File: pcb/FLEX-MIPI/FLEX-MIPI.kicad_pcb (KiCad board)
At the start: 2 copper layers, 2 parts, among them CN1 OK-23GF030-04, J1 Conn_01x22

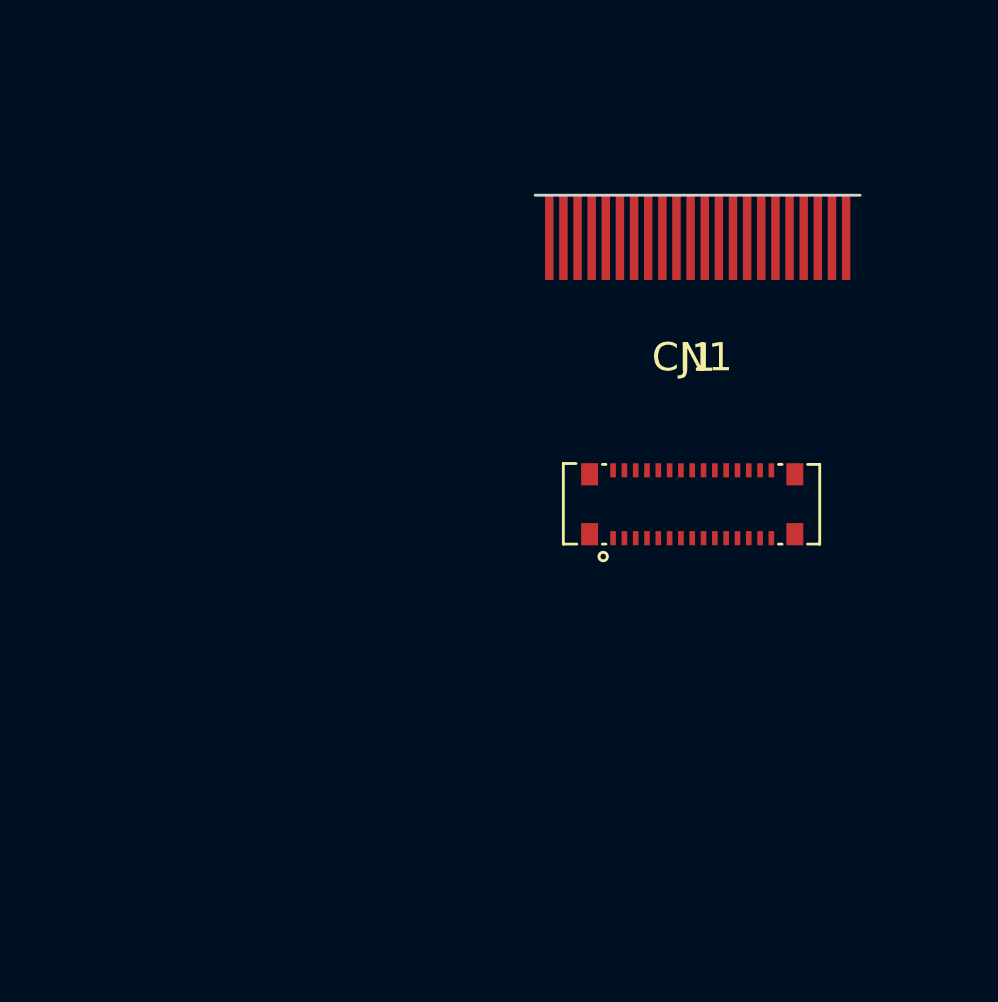
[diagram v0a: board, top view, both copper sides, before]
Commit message: flex mipi work
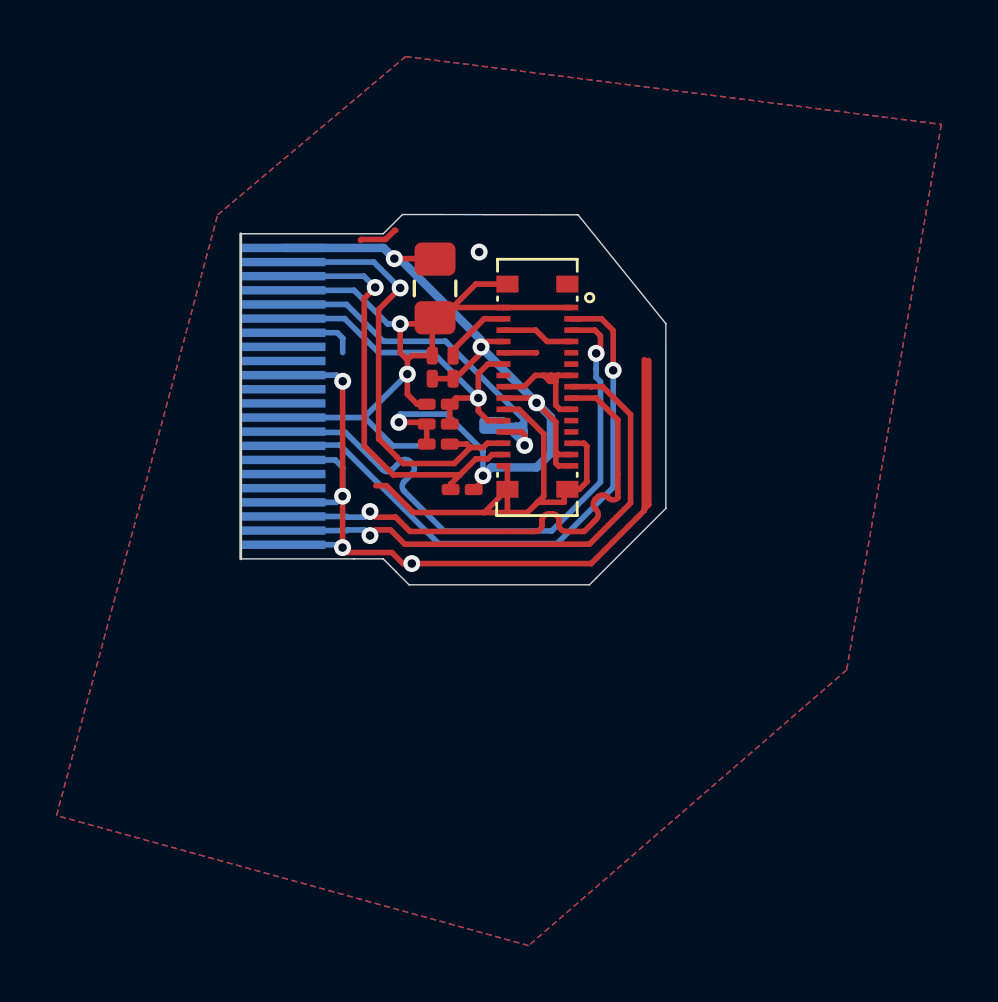
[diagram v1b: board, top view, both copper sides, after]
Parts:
- added C1: 10uF, Capacitor_SMD:C_0805_2012Metric_Pad1.18x1.45mm_HandSolder, F.Cu at (93.7, 53.1)
- added C2: 0.1uF, Capacitor_SMD:C_0201_0603Metric_Pad0.64x0.40mm_HandSolder, F.Cu at (93.6, 55.9)
- added C3: 0.1uF, Capacitor_SMD:C_0201_0603Metric_Pad0.64x0.40mm_HandSolder, F.Cu at (93.8, 57.2)
- added R1: R, Resistor_SMD:R_0201_0603Metric_Pad0.64x0.40mm_HandSolder, F.Cu at (94.6, 60.2)
- added R2: R, Resistor_SMD:R_0201_0603Metric_Pad0.64x0.40mm_HandSolder, F.Cu at (93.8, 58.6)
- added R3: R, Resistor_SMD:R_0201_0603Metric_Pad0.64x0.40mm_HandSolder, F.Cu at (94.3, 55.9)
- added R4: R, Resistor_SMD:R_0201_0603Metric_Pad0.64x0.40mm_HandSolder, F.Cu at (93.8, 57.9)
- added TP1: TestPoint, TestPoint_SMD_1.0x0.6mm_Flex:TestPoint_SMD_1.0x0.6mm_Flex, B.Cu at (95.8, 58.0)
- J1: moved to B.Cu
- moved J1 17.7 mm to (86.8, 56.9), turned to -90 degrees
- moved CN1 6.88 mm to (97.3, 56.6), turned to 90 degrees
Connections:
- net /CTP_RST renamed /RST
- CN1 pad : (no net) -> GND
- CN1 pad 14: unconnected-(CN1-Pad14) -> /LCM_ID
- CN1 pad 24: /CTP_INT -> /TP_INT
- J1 pad 5: /VCI_EN -> /TP_INT
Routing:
- net GND: track 0.00 -> 95.9 mm, vias 0 -> 7
- net +3V3: track 0.00 -> 32.7 mm, vias 0 -> 5
- net /LCM_CLKN: track 0.00 -> 21.2 mm, vias 0 -> 1
- net /LCM_CLKP: track 0.00 -> 21.1 mm, vias 0 -> 1
- net /LCM_D0N: track 0.00 -> 18.9 mm, vias 0 -> 1
- net /LCM_D0P: track 0.00 -> 18.8 mm, vias 0 -> 1
- net /TP_INT: track 0.00 -> 17.6 mm, vias 0 -> 1
- net /TP_TWI2_SDA: track 0.00 -> 16.0 mm, vias 0 -> 1
- net /TP_TWI2_SCK: track 0.00 -> 15.5 mm, vias 0 -> 1
- net /RST: track 0.00 -> 13.3 mm, vias 0 -> 1
- net /VCI_EN: track 0.00 -> 2.44 mm
- added copper zone on B.Cu, net GND
- added copper zone on F.Cu, net GND
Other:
- board outline added: 15 x 13.1 mm

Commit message: pcb fixes
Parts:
- removed TP1: TestPoint, TestPoint_SMD_1.0x0.6mm_Flex:TestPoint_SMD_1.0x0.6mm_Flex
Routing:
- net /TP_INT: track 17.6 -> 13.4 mm
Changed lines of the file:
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@@
 		)
-	)
-	(footprint "TestPoint_SMD_1.0x0.6mm_Flex:TestPoint_SMD_1.0x0.6mm_Flex"
-		(layer "B.Cu")
-		(at 95.75 57.95)
-		(descr "Compact hand-solder test pad for flex PCB; 1.0 x 0.6 mm rounded copper, 0.10 mm coverlay/mask expansion, no paste aperture")
-		(tags "test point flex FPC hand solder wire compact")
-		(property "Reference" "TP1"
-			(at 0 1.1 180)
-			(layer "B.Fab")
-			(hide yes)
-			(effects
-				(font
-					(size 0.6 0.6)
-					(thickness 0.1)
-				)
-				(justify mirror)
-			)
-		)
-		(property "Value" "TestPoint"
-			(at 0 -1.1 180)
-			(layer "B.Fab")
-			(hide yes)
-			(effects
-				(font
-					(size 0.6 0.6)
-					(thickness 0.1)
-				)
-				(justify mirror)
-			)
-		)
-		(property "Datasheet" ""
-			(at 0 0 180)
-			(layer "B.Fab")
-			(hide yes)
-			(effects
-				(font
-					(size 1.27 1.27)
-				)
-				(justify mirror)
-			)
-		)
-		(property "Description" "test point"
-			(at 0 0 180)
-			(layer "B.Fab")
-			(hide yes)
-			(effects
-				(font
-					(size 1.27 1.27)
-				)
-				(justify mirror)
-			)
-		)
-		(property ki_fp_filters "Pin* Test*")
-		(sheetname "/")
-		(sheetfile "FLEX-MIPI.kicad_sch")
-		(units
-			(unit
-				(name "A")
-				(pins "1")
-			)
-		)
-		(attr smd)
-		(duplicate_pad_numbers_are_jumpers no)
-		(pad "1" smd roundrect
-			(at 0 0)
-			(size 1 0.6)
-			(layers "B.Cu" "B.Mask")
-			(roundrect_rratio 0.25)
-			(net "/TP_INT")
-			(pinfunction "1_1")
-			(pintype "passive")
-			(solder_mask_margin 0.1)
-		)
-		(embedded_fonts no)
 	)
 	(footprint "Flex_Tails:FPC_Tail_22P_P0.5"
@@
 	(segment
 		(start 96.860002 58.657258)
-		(end 97.028 58.48926)
-		(width 0.2)
-		(layer "B.Cu")
-		(net "/TP_INT")
-	)
-	(segment
-		(start 96.860002 58.657258)
 		(end 96.860002 58.260002)
-		(width 0.2)
-		(layer "B.Cu")
-		(net "/TP_INT")
-	)
-	(segment
-		(start 95.75 57.95)
-		(end 96.3 57.95)
-		(width 0.2)
-		(layer "B.Cu")
-		(net "/TP_INT")
-	)
-	(segment
-		(start 96.681475 57.95)
-		(end 96.860002 57.771473)
 		(width 0.2)
 		(layer "B.Cu")
@@
 	)
 	(segment
-		(start 96.857258 58.657258)
-		(end 96.3 58.1)
-		(width 0.2)
-		(layer "B.Cu")
-		(net "/TP_INT")
-	)
-	(segment
 		(start 96.860002 58.657258)
 		(end 96.860002 58.128527)
@@
 	)
 	(segment
-		(start 95.75 57.95)
-		(end 96.55 57.95)
-		(width 0.2)
-		(layer "B.Cu")
-		(net "/TP_INT")
-	)
-	(segment
 		(start 94.060529 54.972)
 		(end 96.860002 57.771473)
@@
 	)
 	(segment
-		(start 96.55 57.95)
-		(end 96.681475 57.95)
-		(width 0.2)
-		(layer "B.Cu")
-		(net "/TP_INT")
-	)
-	(segment
 		(start 96.860002 58.657258)
 		(end 96.857258 58.657258)
@@
 		(width 0.2)
 		(layer "B.Cu")
-		(net "/TP_INT")
-	)
-	(segment
-		(start 96.3 57.95)
-		(end 96.860002 58.510002)
-		(width 0.2)
-		(layer "B.Cu")
-		(net "/TP_INT")
-	)
-	(segment
-		(start 96.860002 58.260002)
-		(end 96.55 57.95)
-		(width 0.2)
-		(layer "B.Cu")
-		(net "/TP_INT")
-	)
-	(segment
-		(start 96.860002 58.128527)
-		(end 96.681475 57.95)
-		(width 0.2)
-		(layer "B.Cu")
